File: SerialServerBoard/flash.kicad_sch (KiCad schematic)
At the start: 0 parts

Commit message: Add ESP32-C3 footprint
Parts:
- added J7: Amphenol 10067099-400LF, symbol Connector:Micro_SD_Card_Det2
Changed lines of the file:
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@@
 	(generator_version "8.0")
 	(paper "A4")
+	(symbol
+		(lib_id "Connector:Micro_SD_Card_Det2")
+		(at 256.54 41.91 0)
+		(unit 1)
+		(exclude_from_sim no)
+		(in_bom yes)
+		(on_board yes)
+		(dnp no)
+		(fields_autoplaced yes)
+		(property "Reference" "J7"
+			(at 257.175 20.32 0)
+			(effects
+				(font
+					(size 1.27 1.27)
+				)
+			)
+		)
+		(property "Value" "Amphenol 10067099-400LF"
+			(at 257.175 22.86 0)
+			(effects
+				(font
+					(size 1.27 1.27)
+				)
+			)
+		)
+		(property "Footprint" ""
+			(at 308.61 24.13 0)
+			(effects
+				(font
+					(size 1.27 1.27)
+				)
+				(hide yes)
+			)
+		)
+		(property "Datasheet" "https://www.hirose.com/en/product/document?clcode=&productname=&series=DM3&documenttype=Catalog&lang=en&documentid=D49662_en"
+			(at 259.08 39.37 0)
+			(effects
+				(font
+					(size 1.27 1.27)
+				)
+				(hide yes)
+			)
+		)
+		(property "Description" "Micro SD Card Socket with two card detection pins"
+			(at 256.54 41.91 0)
+			(effects
+				(font
+					(size 1.27 1.27)
+				)
+				(hide yes)
+			)
+		)
+		(pin "8"
+		)
+		(pin "7"
+		)
+		(pin "4"
+		)
+		(pin "3"
+		)
+		(pin "6"
+		)
+		(pin "1"
+		)
+		(pin "5"
+		)
+		(pin "2"
+		)
+		(pin "9"
+		)
+		(pin "10"
+		)
+		(pin "11"
+		)
+		(instances
+			(project "SerialServerBoard"
+				(path "/fff4edd7-7765-4881-b8c8-325c8be7c8ba/1a3105c5-9a28-4570-b6a0-d07c3a3e2a73"
+					(reference "J7")
+					(unit 1)
+				)
+			)
+		)
+	)
 )

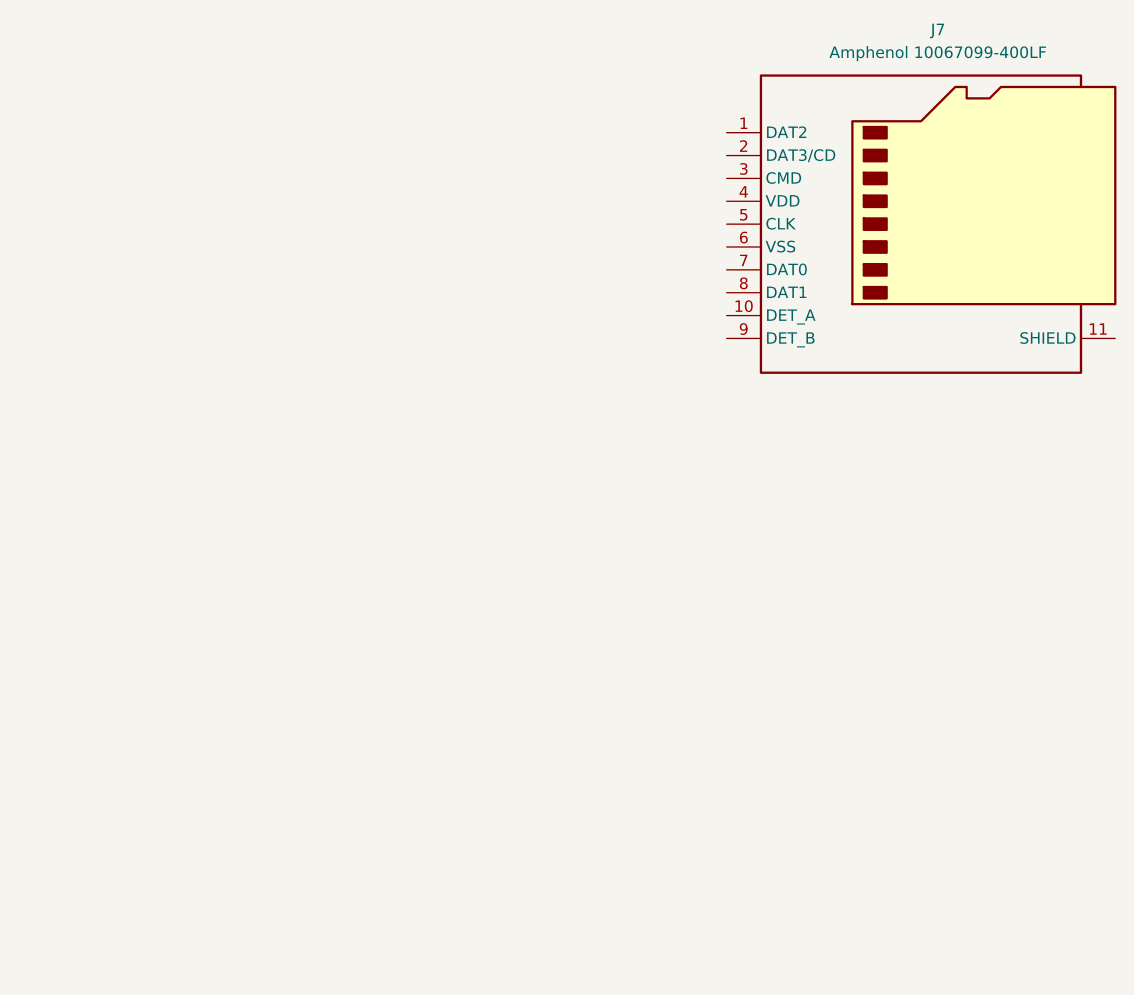
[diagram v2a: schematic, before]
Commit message: Add micro-SD card slot
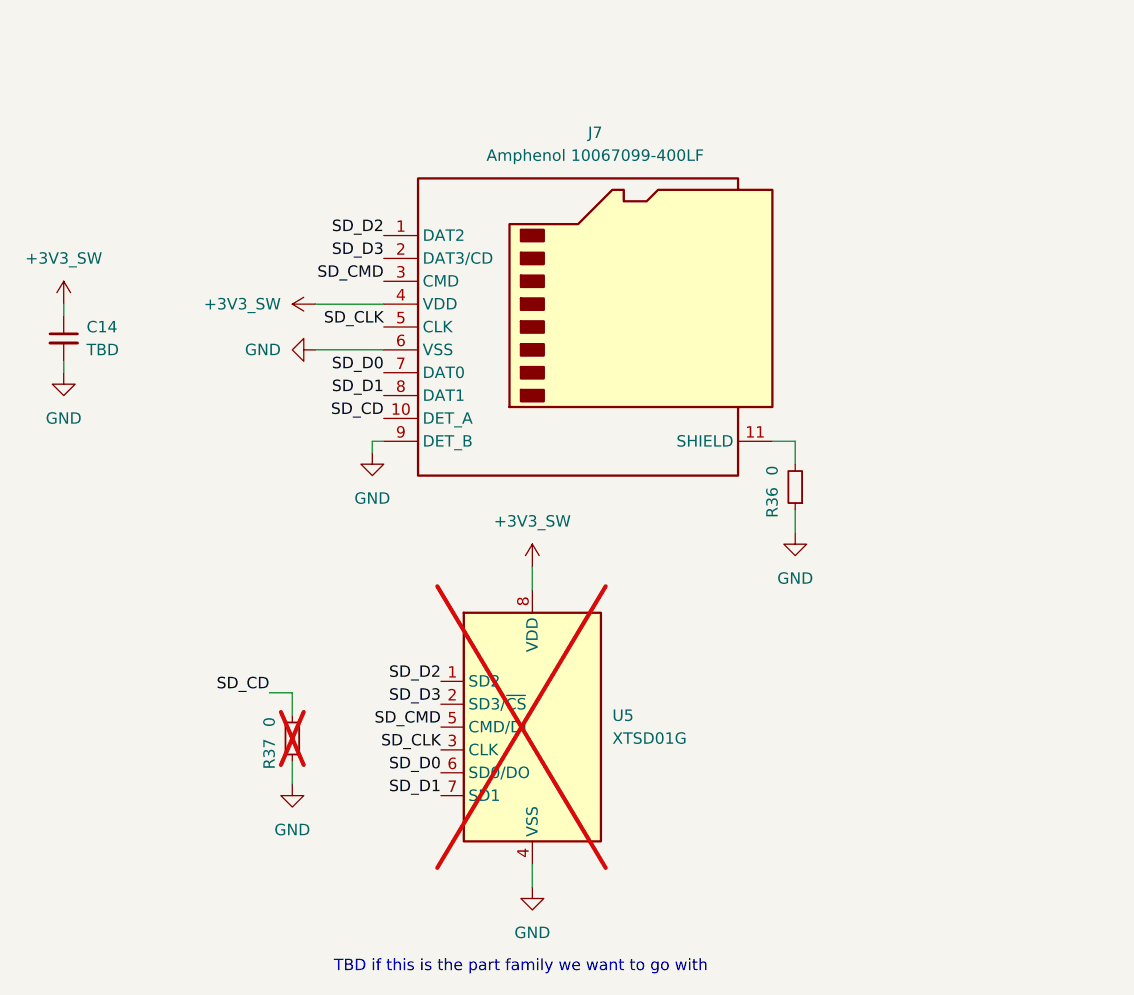
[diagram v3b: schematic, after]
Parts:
- added C14: TBD, Capacitor_SMD:C_0603_1608Metric, symbol Device:C_Small
- added R36, R37: 0, Resistor_SMD:R_0402_1005Metric, symbol Device:R_Small
- added U5: XTSD01G, Package_LGA:LGA-8_8x6mm_P1.27mm, symbol Memory_Flash:XTSD01G
- J7: footprint (none) -> Footprints:CONN8_10067099-400LF_FCI
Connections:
- net SD_D2: now reaches J7.1 (DAT2)
- net SD_D2: now also U5.1 (SD2)
- net SD_CD: now reaches J7.10 (DET_A)
- net SD_CD: now also R37.2
- net at J7.11 (SHIELD): now also R36.2
- net SD_D3: now reaches J7.2 (DAT3/CD)
- net SD_D3: now also U5.2 (SD3/~{CS})
- net SD_CMD: now reaches J7.3 (CMD)
- net SD_CMD: now also U5.5 (CMD/DI)
- net +3V3_SW: now reaches J7.4 (VDD)
- net +3V3_SW: now also C14.1, U5.8 (VDD)
- net SD_CLK: now reaches J7.5 (CLK)
- net SD_CLK: now also U5.3 (CLK)
- net GND: now reaches J7.6 (VSS)
- net GND: now also J7.9 (DET_B), C14.2, R36.1, R37.1, U5.4 (VSS)
- net SD_D0: now reaches J7.7 (DAT0)
- net SD_D0: now also U5.6 (SD0/DO)
- net SD_D1: now reaches J7.8 (DAT1)
- net SD_D1: now also U5.7 (SD1)
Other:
- note added: "TBD if this is the part family we want to go with"
- moved on the sheet: J7
